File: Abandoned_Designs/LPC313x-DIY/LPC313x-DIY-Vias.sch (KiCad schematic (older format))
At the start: 123 parts

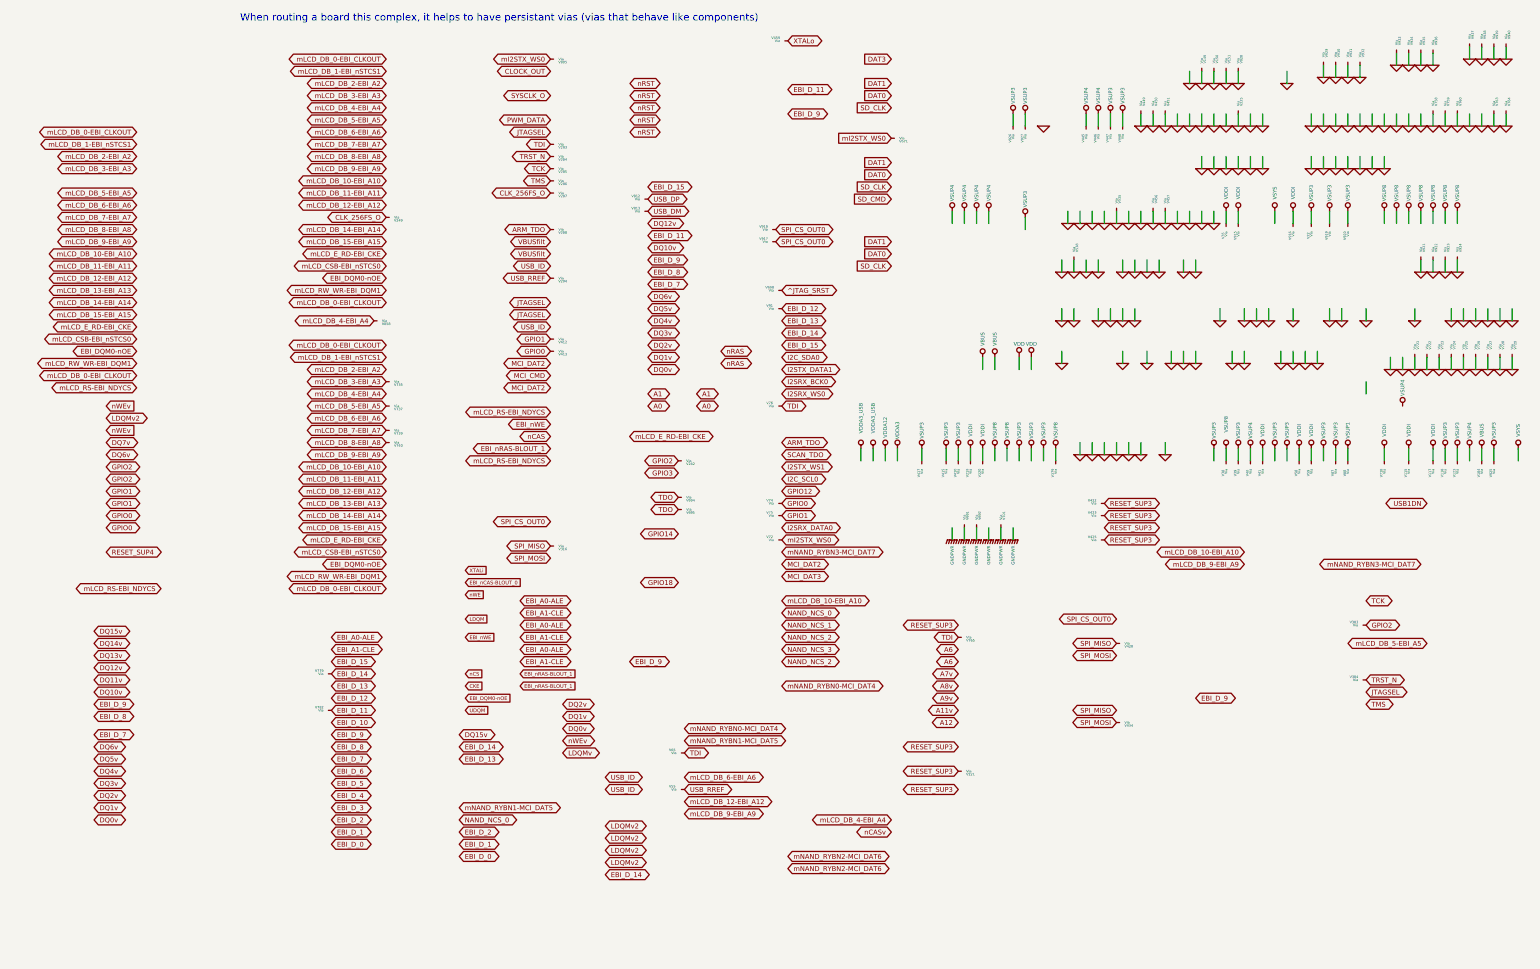
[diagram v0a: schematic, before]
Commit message: Updated LPC313x DIY board to a larger board size to fix PCB manufacturing issues.
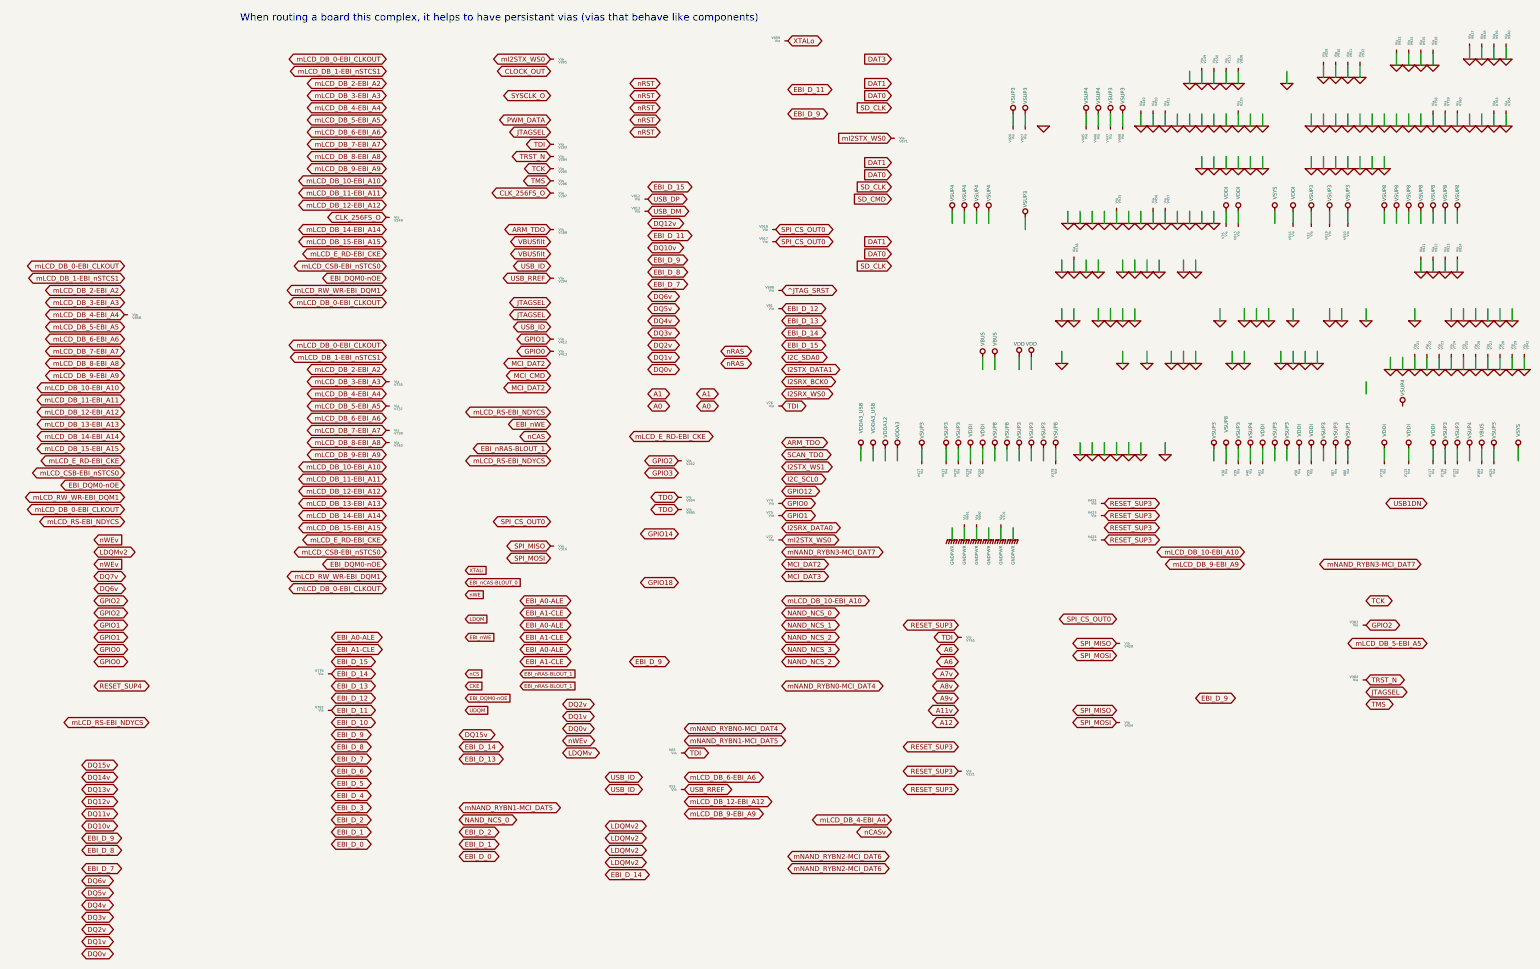
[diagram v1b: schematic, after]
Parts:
- added V941: VIA, symbol VIA
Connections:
- wire segments 209 -> 210
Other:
- moved on the sheet: V858
